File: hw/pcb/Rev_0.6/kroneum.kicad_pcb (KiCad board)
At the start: 2 copper layers, 40 x 40 mm, 25 parts, among them J1 USB_B_Micro, SW1 Boot_Mode_Btn, SW2 Ctrl_One_Btn, SW3 Reset_Btn, SW4 Ctrl_Ten_Btn, U1 STM32F042F4Px, U2 MCP1700-3302E_SOT89

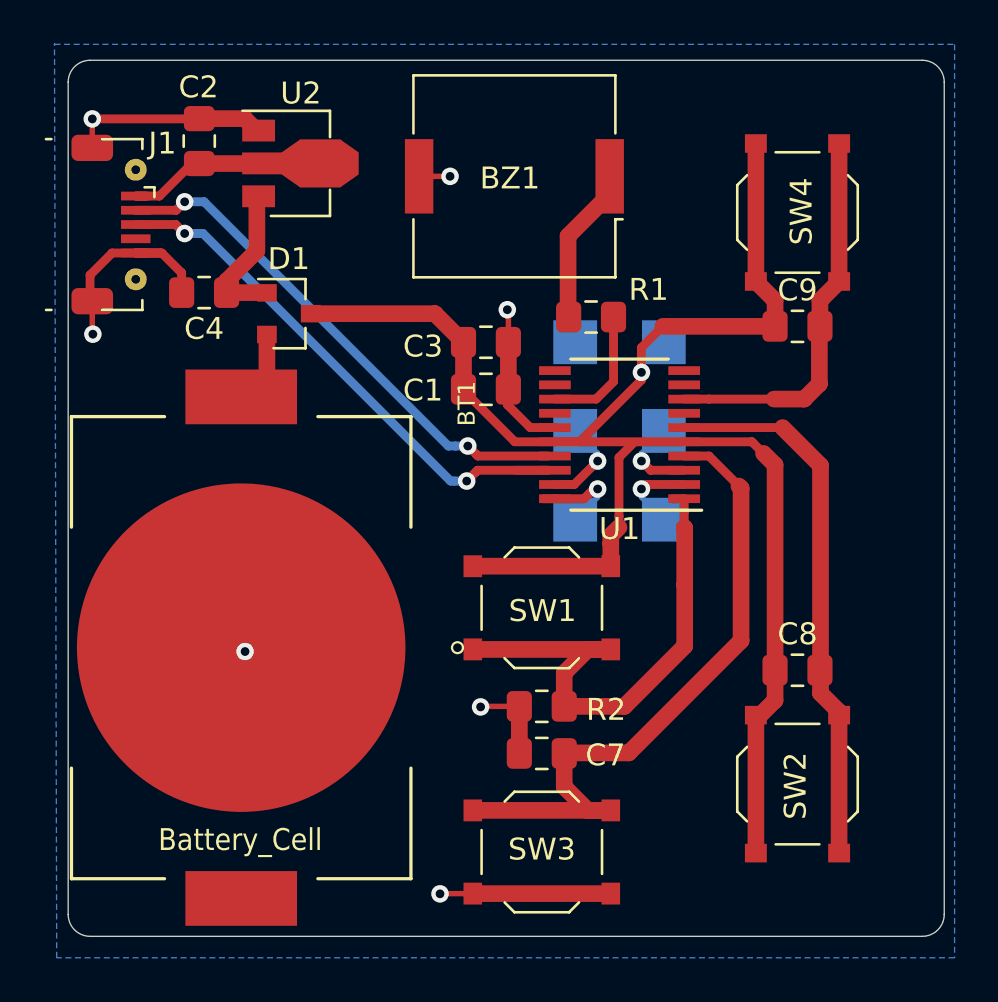
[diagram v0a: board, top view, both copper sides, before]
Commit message: [pcb] introduce PCB rev 0.6 (reduced size to 30mmx30mm, exposed all unused pads, moved batter to the back layer)
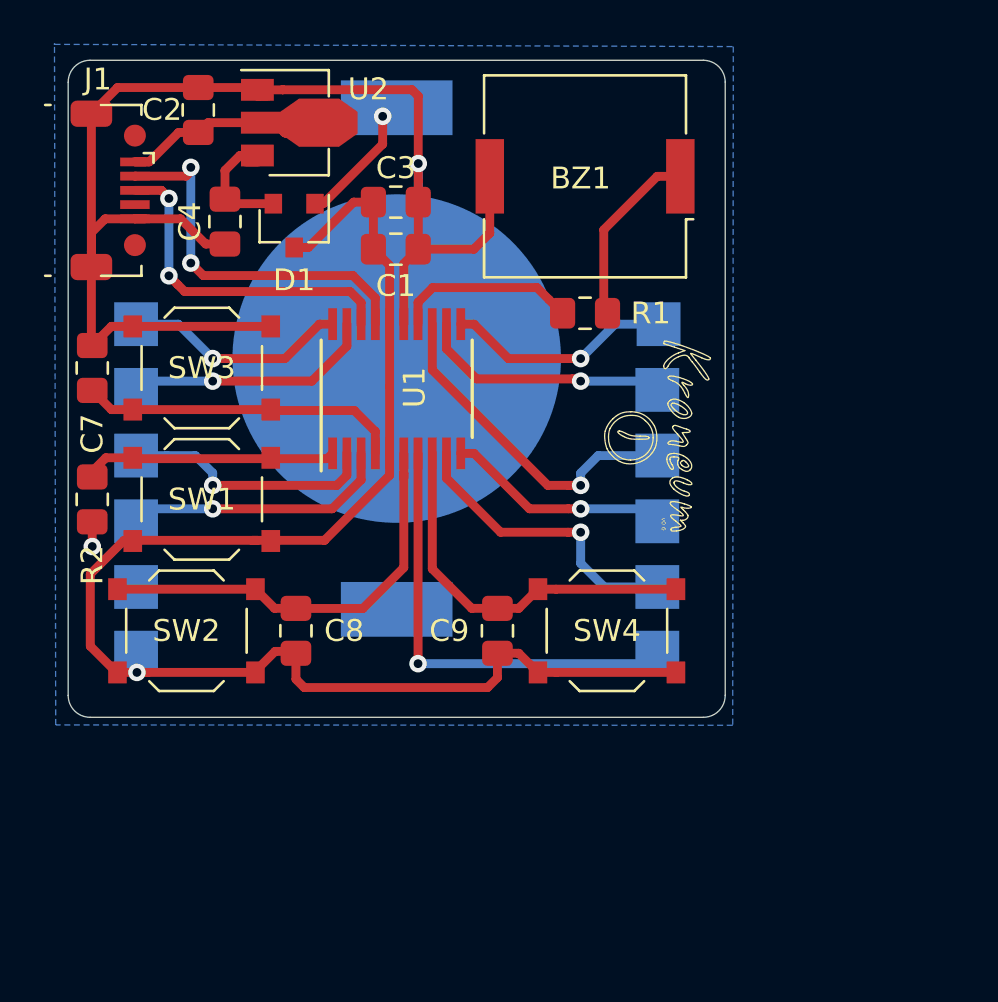
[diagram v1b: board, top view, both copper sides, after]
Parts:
- added ADC1: Peripherals, TestPoint:TestPoint_THTPad_2.0x2.0mm_Drill1.0mm, B.Cu at (153.3, 120.0)
- added ADC3: Peripherals, TestPoint:TestPoint_THTPad_2.0x2.0mm_Drill1.0mm, B.Cu at (153.3, 117.0)
- added MISO: Peripherals, TestPoint:TestPoint_THTPad_2.0x2.0mm_Drill1.0mm, B.Cu at (153.3, 108.0)
- added MOSI: Peripherals, TestPoint:TestPoint_THTPad_2.0x2.0mm_Drill1.0mm, B.Cu at (153.3, 111.0)
- added NSS: Peripherals, TestPoint:TestPoint_THTPad_2.0x2.0mm_Drill1.0mm, B.Cu at (153.3, 114.0)
- added SCK: Peripherals, TestPoint:TestPoint_THTPad_2.0x2.0mm_Drill1.0mm, B.Cu at (153.3, 105.0)
- BT1: value Battery_Cell -> Battery; moved to B.Cu
- moved SW2 28.8 mm to (131.8, 119.0), turned to 0 degrees
- moved VDD 28.0 mm to (129.5, 120.0)
- moved C7 27.0 mm to (127.5, 107.0), turned to 90 degrees
- moved SW3 27.0 mm to (132.5, 107.0), turned to 180 degrees
- moved SCL 24.5 mm to (129.5, 114.0)
- moved SDA 24.3 mm to (129.5, 111.0)
- moved C8 23.0 mm to (136.8, 119.0), turned to 90 degrees
- moved GND 23.0 mm to (129.5, 117.0)
- moved R2 22.6 mm to (127.5, 113.0), turned to 270 degrees
- moved SWCLK 21.9 mm to (129.5, 105.0)
- moved SW4 21.0 mm to (151.0, 119.0), turned to 0 degrees
- moved SWDIO 20.1 mm to (129.5, 108.0)
- moved C9 19.5 mm to (146.0, 119.0), turned to 90 degrees
- moved SW1 16.3 mm to (132.5, 113.0), turned to 0 degrees
- moved BT1 15.0 mm to (141.4, 106.6), turned to 90 degrees
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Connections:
- D1 pad 1: Net-(C4-Pad1) -> Net-(BT1-Pad1)
- D1 pad 2: Net-(BT1-Pad1) -> Net-(C4-Pad1)
- U1 pad 10: Net-(U1-Pad10) -> NSS
- U1 pad 11: Net-(U1-Pad11) -> SCK
- U1 pad 12: Net-(U1-Pad12) -> MISO
- U1 pad 13: Buzzer -> MOSI
- U1 pad 14: Net-(U1-Pad14) -> Buzzer
- U1 pad 7: Net-(U1-Pad7) -> ADC1
- U1 pad 9: Net-(U1-Pad9) -> ADC3
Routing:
- net GND: track 42.9 -> 73.2 mm, vias 7 -> 2
- net ADC1: track 0.00 -> 20.7 mm, vias 0 -> 1
- net NRST: track 30.7 -> 14.3 mm
- net MOSI: track 0.00 -> 15.4 mm, vias 0 -> 1
- net ADC3: track 0.00 -> 13.6 mm, vias 0 -> 1
- net BOOT0: track 24.3 -> 11.6 mm
- net VDD: track 79.2 -> 67.7 mm
- net MISO: track 0.00 -> 11.5 mm, vias 0 -> 1
- net SCK: track 0.00 -> 10.3 mm, vias 0 -> 1
- net NSS: track 0.00 -> 10.3 mm, vias 0 -> 1
- net USB_D+: track 25.4 -> 15.6 mm
- net SCL: track 3.92 -> 12.3 mm
- net SDA: track 3.86 -> 11.7 mm
- net SWDIO: track 4.19 -> 11.5 mm
- net USB_D-: track 23.8 -> 17.6 mm
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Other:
- board size 40 x 40 mm -> 30 x 30 mm
- board text added: "v0.6"
